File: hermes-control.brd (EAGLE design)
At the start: 106 x 47 mm, 73 parts, among them J1 1981568-1, J3 2201778-1, Q2 BC849SMD, Q3 FDN360P, Q4 FDN360P, Q5 BC849SMD, Q6 MMBT3906SOT23-3, Q7 FDN360P, Q8 MMBT2222A, U1 LSM9DS1TR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

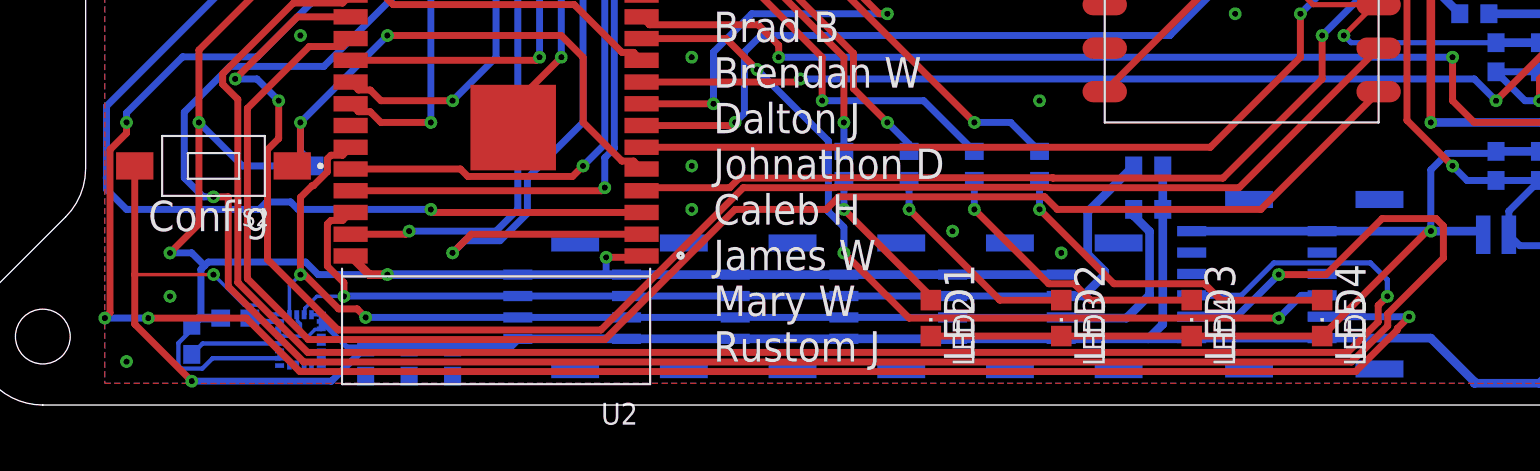
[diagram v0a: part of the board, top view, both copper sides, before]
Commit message: more gnd
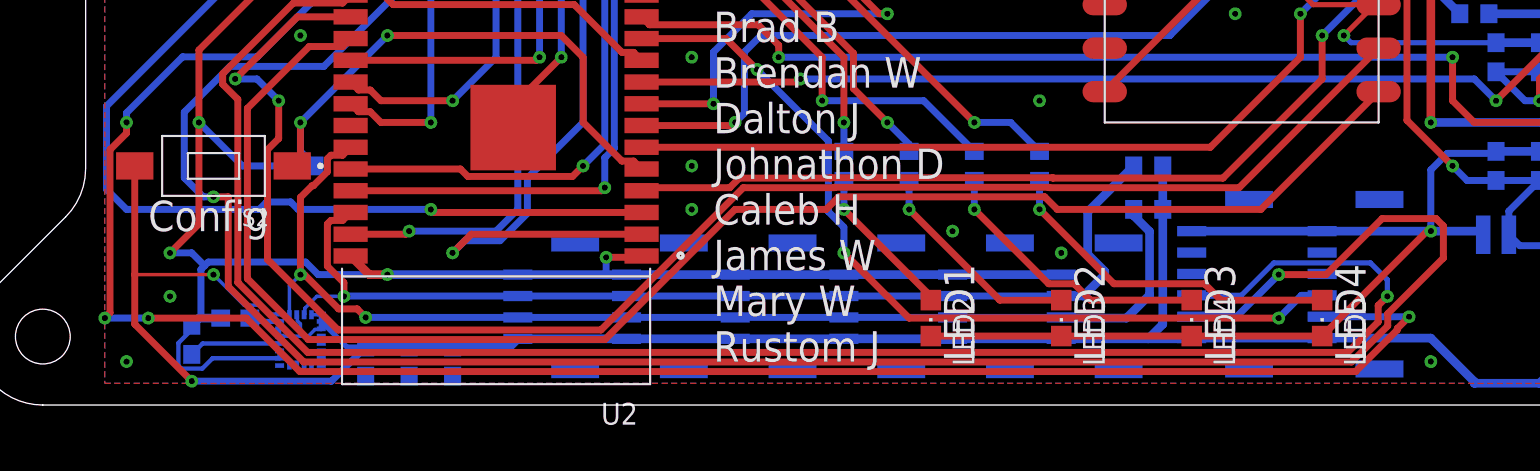
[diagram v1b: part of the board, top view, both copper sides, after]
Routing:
- net GND: vias 46 -> 47
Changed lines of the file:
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@@
 <via x="63.5" y="8.89" extent="1-16" drill="0.35"/>
 <via x="19.05" y="21.59" extent="1-16" drill="0.35"/>
-<wire x1="17.83" y1="2.735" x2="22.86" y2="1.69" width="0" layer="19" extent="16-16"/>
+<via x="85.09" y="2.54" extent="1-16" drill="0.35"/>
 </signal>
 <signal name="3.3V">
@@
 <wire x1="17.08270625" y1="11.8656" x2="16.64710625" y2="11.43" width="0.4064" layer="16"/>
 <wire x1="7.72056875" y1="17.46056875" x2="19.05" y2="28.79" width="0.4064" layer="16"/>
-<wire x1="7.70100625" y1="13.2770875" x2="7.72056875" y2="13.29665" width="0.4064" layer="16"/>
-<wire x1="7.72056875" y1="13.29665" x2="7.72056875" y2="17.46056875" width="0.4064" layer="16"/>
 <wire x1="8.89" y1="11.43" x2="7.72056875" y2="12.59943125" width="0.4064" layer="16"/>
-<wire x1="7.72056875" y1="12.59943125" x2="7.72056875" y2="13.29665" width="0.4064" layer="16"/>
+<wire x1="7.72056875" y1="12.59943125" x2="7.72056875" y2="17.46056875" width="0.4064" layer="16"/>
 </signal>
 <signal name="N$19">

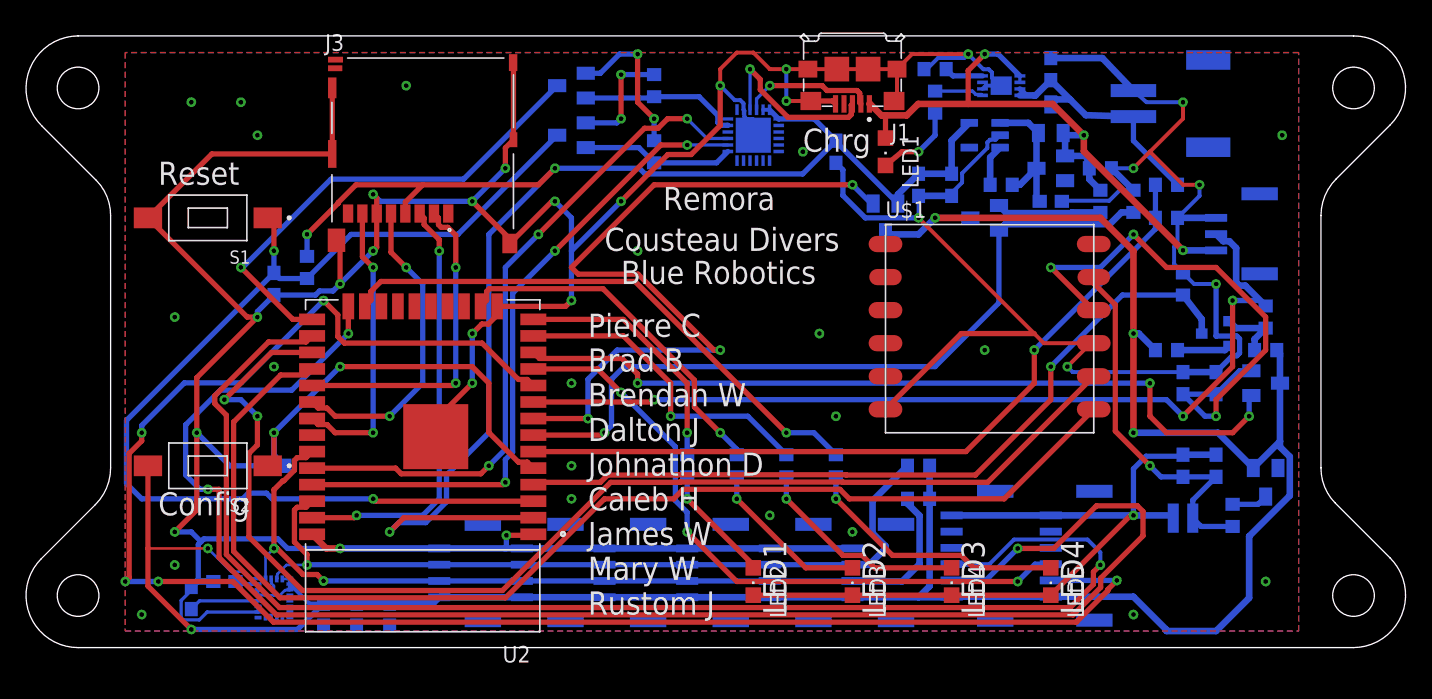
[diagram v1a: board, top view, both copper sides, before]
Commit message: flip sd card and connect vcc to usb uart chip
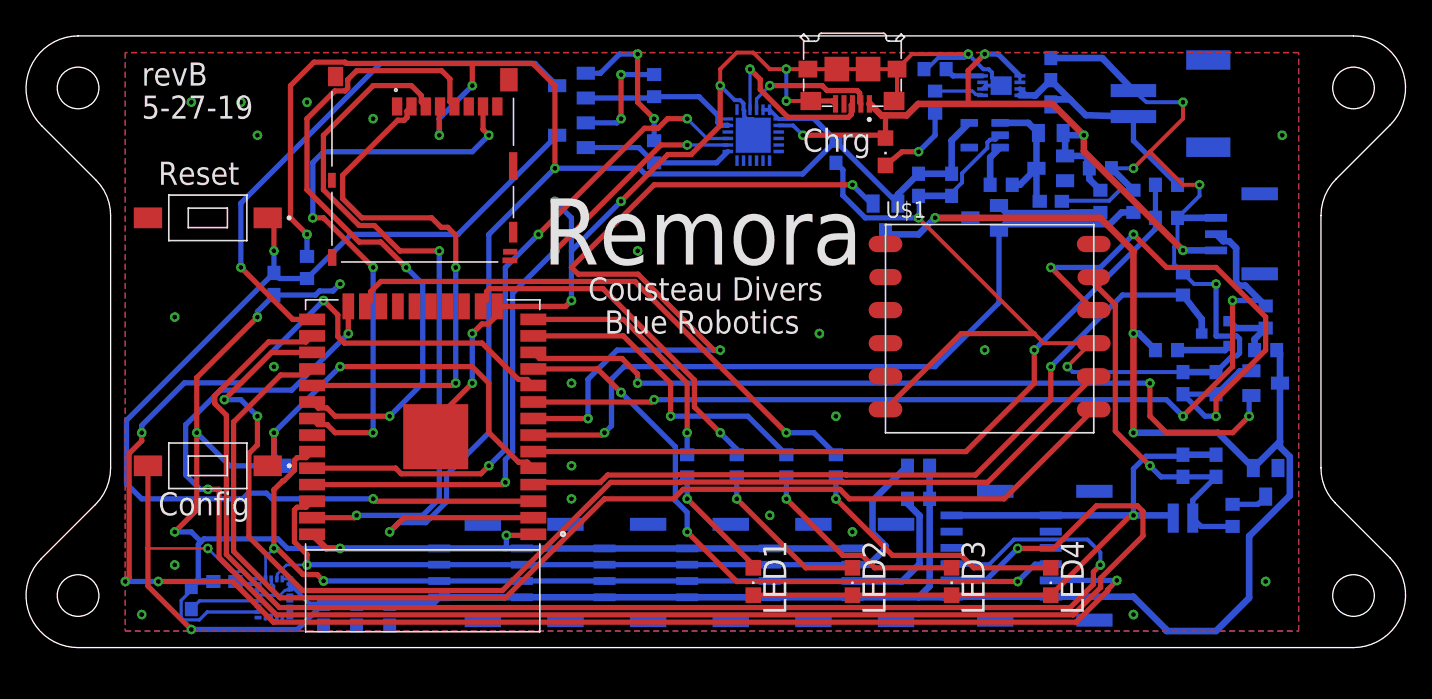
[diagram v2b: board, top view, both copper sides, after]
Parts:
- moved J3 1.27 mm to (30.5, 36.8), turned to 180 degrees
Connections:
- removed net N$11: U3.8
- net VCC: now also U3.8
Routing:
- net GND: track 451.1 -> 377.5 mm, vias 47 -> 43
- net CLK: track 24.0 -> 50.4 mm
- net VCCIO: track 117.7 -> 142.7 mm, vias 3 -> 5
- net MISO: track 22.3 -> 45.1 mm, vias 2 -> 4
- net MOSI: track 32.9 -> 54.9 mm
- net CS: track 25.1 -> 41.9 mm
- net VCC: track 50.9 -> 59.5 mm, vias 3 -> 4
- net PGM: track 37.2 -> 41.5 mm
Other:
- board text added: "5-27-19"
- board text added: "revB"
- board text removed: "Pierre C Brad B Brendan W Dalton J Johnathon D Caleb H James W Mary W Rustom J"

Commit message: new bat connector
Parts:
- LBAT: value S2B-PH-SM4-TB(LF)(SN) -> B2B-PH-SM4-TB(LF)(SN); device hermes:JST_S2B-PH-SM4-TB(LF)(SN) -> B2B-PH-SM4-TB_LF__SN_:JST_B2B-PH-SM4-TB(LF)(SN)
- moved LBAT 7.73 mm to (92.7, 40.5), turned to 0 degrees
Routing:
- net GND: track 377.5 -> 387.6 mm
- net V_BATT: track 19.9 -> 25.7 mm
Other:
- board text added: "5-31-19"
- board text removed: "5-27-19"
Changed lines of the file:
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@@
 <drawing>
 <settings>
-<setting alwaysvectorfont="no"/>
+<setting alwaysvectorfont="yes"/>
 <setting verticaltext="up"/>
 </settings>
-<grid distance="50" unitdist="mil" unit="mil" style="lines" multiple="1" display="yes" altdistance="5" altunitdist="mil" altunit="mil"/>
+<grid distance="50" unitdist="mil" unit="mm" style="lines" multiple="1" display="yes" altdistance="5" altunitdist="mil" altunit="mm"/>
 <layers>
 <layer number="1" name="Top" color="4" fill="1" visible="yes" active="yes"/>
@@
 <text x="81.28" y="2.54" size="1.778" layer="21" rot="R90">LED4</text>
 <text x="8.89" y="43.18" size="1.778" layer="21">revB</text>
-<text x="8.89" y="40.64" size="1.778" layer="21">5-27-19</text>
+<text x="8.89" y="40.64" size="1.778" layer="21">5-31-19</text>
 </plain>
 <attributes>
@@
 <attribute name="VALUE" x="38.10573125" y="47.506" size="1.270959375" layer="27" rot="R180"/>
 </element>
-<element name="LBAT" library="hermes" package="JST_S2B-PH-SM4-TB(LF)(SN)" value="S2B-PH-SM4-TB(LF)(SN)" x="85.09" y="41.8" smashed="yes" rot="MR270">
-<attribute name="MANUFACTURER" value="JST" x="85.09" y="41.8" size="1.778" layer="28" rot="MR270" display="off"/>
-<attribute name="NAME" x="82.542390625" y="45.67423125" size="1.27278125" layer="26" rot="MR270"/>
-<attribute name="STANDARD" value="Manufacturer Recommendation" x="85.09" y="41.8" size="1.778" layer="28" rot="MR270" display="off"/>
-<attribute name="VALUE" x="95.2087" y="45.55341875" size="1.274540625" layer="28" rot="MR270"/>
+<element name="LBAT" library="B2B-PH-SM4-TB_LF__SN_" package="JST_B2B-PH-SM4-TB(LF)(SN)" value="B2B-PH-SM4-TB(LF)(SN)" x="92.71" y="40.53" smashed="yes" rot="MR0">
+<attribute name="AVAILABILITY" value="Unavailable" x="92.71" y="40.53" size="1.778" layer="28" rot="MR0" display="off"/>
+<attribute name="DESCRIPTION" value=" PH Series 2 Position 2 mm Pitch Surface Mount Top Entry Shrouded Header " x="92.71" y="40.53" size="1.778" layer="28" rot="MR0" display="off"/>
+<attribute name="MF" value="JST Sales" x="92.71" y="40.53" size="1.778" layer="28" rot="MR0" display="off"/>
+<attribute name="MP" value="B2B-PH-SM4-TB_LF__SN_" x="92.71" y="40.53" size="1.778" layer="28" rot="MR0" display="off"/>
+<attribute name="NAME" x="96.58423125" y="43.077609375" size="1.27278125" layer="26" rot="MR0"/>
+<attribute name="PACKAGE" value="None" x="92.71" y="40.53" size="1.778" layer="28" rot="MR0" display="off"/>
+<attribute name="PRICE" value="None" x="92.71" y="40.53" size="1.778" layer="28" rot="MR0" display="off"/>
+<attribute name="VALUE" x="96.46341875" y="30.4113" size="1.274540625" layer="28" rot="MR0"/>
 </element>
 <element name="R24" library="rcl" library_urn="urn:adsk.eagle:library:334" package="R0603" package3d_urn="urn:adsk.eagle:package:23555/3" value="1k" x="69.85" y="41.91" smashed="yes" rot="MR90">
@@
 <wire x1="13.12" y1="5.08" x2="14.39" y2="5.08" width="0.508" layer="16"/>
 <wire x1="13.12" y1="5.08" x2="12.7" y2="4.66" width="0.508" layer="16"/>
-<wire x1="85.09" y1="42.8" x2="82.7" y2="45.3" width="0.508" layer="16"/>
-<wire x1="82.7" y1="45.3" x2="78.74" y2="45.3" width="0.508" layer="16"/>
 <wire x1="84.03105" y1="35.14" x2="85.09" y2="35.14" width="0.3048" layer="16"/>
 <wire x1="83.22625" y1="34.3352" x2="84.03105" y2="35.14" width="0.3048" layer="16"/>
@@
 <via x="85.09" y="36.83" extent="1-16" drill="0.35"/>
 <wire x1="85.09" y1="36.83" x2="86.36" y2="38.1" width="0.3048" layer="1"/>
-<wire x1="86.36" y1="38.1" x2="88.9" y2="40.64" width="0.3048" layer="1"/>
-<wire x1="88.9" y1="40.64" x2="88.9" y2="41.91" width="0.3048" layer="1"/>
-<via x="88.9" y="41.91" extent="1-16" drill="0.35"/>
-<wire x1="88.9" y1="41.91" x2="86.09" y2="41.91" width="0.3048" layer="16"/>
-<wire x1="86.09" y1="41.91" x2="85.09" y2="42.8" width="0.3048" layer="16"/>
+<via x="82.55" y="41.91" extent="1-16" drill="0.35"/>
 <wire x1="88.48" y1="33.02" x2="90.17" y2="34.71" width="0.3048" layer="16"/>
 <wire x1="90.17" y1="34.71" x2="90.17" y2="35.56" width="0.3048" layer="16"/>
@@
 <wire x1="90.17" y1="35.56" x2="88.9" y2="35.56" width="0.3048" layer="1"/>
 <wire x1="88.9" y1="35.56" x2="86.36" y2="38.1" width="0.3048" layer="1"/>
+<wire x1="86.36" y1="38.1" x2="82.55" y2="41.91" width="0.3048" layer="1"/>
 <wire x1="71.9248" y1="35.73375" x2="71.9248" y2="36.4498" width="0.3048" layer="16"/>
 <wire x1="71.9248" y1="36.4498" x2="73.8652" y2="38.3902" width="0.3048" layer="16"/>
@@
 <via x="21.59" y="41.91" extent="1-16" drill="0.35"/>
 <via x="95.25" y="5.08" extent="1-16" drill="0.35"/>
-<via x="96.52" y="39.37" extent="1-16" drill="0.35"/>
+<via x="96.52" y="36.83" extent="1-16" drill="0.35"/>
 <via x="60.96" y="24.13" extent="1-16" drill="0.35"/>
 <via x="73.66" y="22.86" extent="1-16" drill="0.35"/>
@@
 <via x="85.09" y="2.54" extent="1-16" drill="0.35"/>
 <via x="26.67" y="40.64" extent="1-16" drill="0.35"/>
+<wire x1="78.74" y1="45.3" x2="82.13" y2="41.91" width="0.508" layer="16"/>
+<wire x1="82.13" y1="41.91" x2="82.55" y2="41.91" width="0.508" layer="16"/>
+<wire x1="82.55" y1="41.91" x2="83.82" y2="41.91" width="0.508" layer="16"/>
+<wire x1="86.5964" y1="44.6864" x2="92.4736" y2="44.6864" width="0.508" layer="16"/>
+<wire x1="92.4736" y1="44.6864" x2="93.98" y2="43.18" width="0.508" layer="16"/>
+<wire x1="93.98" y1="43.18" x2="93.98" y2="40.8" width="0.508" layer="16"/>
+<wire x1="93.98" y1="40.8" x2="93.71" y2="40.53" width="0.508" layer="16"/>
+<wire x1="83.82" y1="41.91" x2="86.5964" y2="44.6864" width="0.508" layer="16"/>
 </signal>
 <signal name="3.3V">
@@
 <contactref element="Q4" pad="3"/>
 <wire x1="78.74" y1="43.6" x2="80.22" y2="42.12" width="0.508" layer="16"/>
-<wire x1="80.22" y1="42.12" x2="81.43" y2="40.91" width="0.508" layer="16"/>
-<wire x1="81.43" y1="40.91" x2="85.09" y2="40.8" width="0.508" layer="16"/>
 <wire x1="78.74" y1="41.74" x2="79.12" y2="42.12" width="0.508" layer="16"/>
 <wire x1="79.12" y1="42.12" x2="80.22" y2="42.12" width="0.508" layer="16"/>
@@
 <wire x1="77.47" y1="42.43" x2="76.865" y2="42.43" width="0.4064" layer="16"/>
 <wire x1="76.865" y1="42.43" x2="76.365" y2="42.93" width="0.4064" layer="16"/>
-<wire x1="88.48" y1="35.56" x2="85.09" y2="38.95" width="0.4064" layer="16"/>
-<wire x1="85.09" y1="38.95" x2="85.09" y2="40.8" width="0.4064" layer="16"/>
+<wire x1="82.81" y1="39.53" x2="85.09" y2="39.53" width="0.508" layer="16"/>
+<wire x1="86.36" y1="39.53" x2="90.71" y2="39.53" width="0.508" layer="16"/>
+<wire x1="85.09" y1="39.53" x2="86.36" y2="39.53" width="0.508" layer="16"/>
+<wire x1="90.71" y1="39.53" x2="91.71" y2="40.53" width="0.508" layer="16"/>
+<wire x1="80.22" y1="42.12" x2="82.81" y2="39.53" width="0.508" layer="16"/>
+<wire x1="88.48" y1="35.56" x2="86.36" y2="37.68" width="0.508" layer="16"/>
+<wire x1="86.36" y1="37.68" x2="86.36" y2="39.53" width="0.508" layer="16"/>
 </signal>
 <signal name="VCC">

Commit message: flipped fet
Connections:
- net 3.3V: now also Q3.2; no longer Q3.3
- net N$6: now also Q3.3; no longer Q3.2
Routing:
- net 3.3V: track 201.0 -> 206.0 mm
- net N$6: track 43.3 -> 45.4 mm
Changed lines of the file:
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@@
 <?xml version="1.0" encoding="utf-8"?>
 <!DOCTYPE eagle SYSTEM "eagle.dtd">
-<eagle version="9.4.0">
+<eagle version="9.4.2">
 <drawing>
 <settings>
-<setting alwaysvectorfont="yes"/>
+<setting alwaysvectorfont="no"/>
 <setting verticaltext="up"/>
 </settings>
@@
 <contactref element="U1" pad="6"/>
 <contactref element="U1" pad="5"/>
-<contactref element="Q3" pad="3"/>
 <contactref element="U1" pad="1"/>
 <contactref element="U1" pad="3"/>
@@
 <wire x1="71.08" y1="3.87" x2="68.58" y2="3.87" width="0.508" layer="16"/>
 <wire x1="68.58" y1="3.87" x2="63.5" y2="3.87" width="0.508" layer="16"/>
-<wire x1="96.35" y1="20.32" x2="96.35" y2="15.85" width="0.508" layer="16"/>
-<wire x1="96.35" y1="15.85" x2="94.3" y2="13.8" width="0.508" layer="16"/>
 <wire x1="72.56" y1="33.02" x2="69.85" y2="33.02" width="0.508" layer="16"/>
 <wire x1="69.85" y1="33.02" x2="68.58" y2="31.75" width="0.508" layer="16"/>
@@
 <wire x1="66.04" y1="31.92" x2="66.2164" y2="31.7436" width="0.508" layer="16"/>
 <wire x1="96.1" y1="22.86" x2="96.35" y2="22.61" width="0.508" layer="16"/>
-<wire x1="96.35" y1="22.61" x2="96.35" y2="20.32" width="0.508" layer="16"/>
 <wire x1="69.43" y1="13.97" x2="69.43" y2="11.43" width="0.508" layer="16"/>
 <wire x1="69.43" y1="11.43" x2="69.43" y2="4.72" width="0.508" layer="16"/>
@@
 <wire x1="18.871" y1="4.91553125" x2="19.05" y2="4.73653125" width="0.2032" layer="16"/>
 <wire x1="97.1064" y1="11.6816625" x2="97.1064" y2="14.6683375" width="0.508" layer="16"/>
-<wire x1="96.35" y1="15.85" x2="96.35" y2="15.4247375" width="0.508" layer="16"/>
-<wire x1="97.1064" y1="14.6683375" x2="96.35" y2="15.4247375" width="0.508" layer="16"/>
 <wire x1="94.3" y1="13.8" x2="91.59" y2="16.51" width="0.508" layer="16"/>
 <wire x1="91.59" y1="16.51" x2="85.09" y2="16.51" width="0.508" layer="16"/>
@@
 <wire x1="93.98" y1="8.5552625" x2="97.1064" y2="11.6816625" width="0.508" layer="16"/>
 <wire x1="93.98" y1="3.8115" x2="93.98" y2="8.5552625" width="0.508" layer="16"/>
+<contactref element="Q3" pad="2"/>
+<wire x1="95.74" y1="22.86" x2="96.1" y2="22.86" width="0.4064" layer="16"/>
+<wire x1="94.15" y1="21.27" x2="94.8344" y2="21.9544" width="0.4064" layer="16"/>
+<wire x1="94.8344" y1="21.9544" x2="95.04729375" y2="21.9544" width="0.4064" layer="16"/>
+<wire x1="95.04729375" y1="21.9544" x2="95.2556" y2="22.16270625" width="0.4064" layer="16"/>
+<wire x1="95.2556" y1="22.16270625" x2="95.2556" y2="22.3756" width="0.4064" layer="16"/>
+<wire x1="95.2556" y1="22.3756" x2="95.74" y2="22.86" width="0.4064" layer="16"/>
+<wire x1="96.35" y1="15.4247375" x2="96.35" y2="19.07" width="0.4064" layer="16"/>
+<wire x1="97.19729375" y1="21.1756" x2="97.4056" y2="20.96729375" width="0.4064" layer="16"/>
+<wire x1="97.4056" y1="20.96729375" x2="97.4056" y2="19.67270625" width="0.4064" layer="16"/>
+<wire x1="97.4056" y1="19.67270625" x2="97.19729375" y2="19.4644" width="0.4064" layer="16"/>
+<wire x1="94.15" y1="21.27" x2="94.2444" y2="21.1756" width="0.4064" layer="16"/>
+<wire x1="97.19729375" y1="19.4644" x2="96.7444" y2="19.4644" width="0.4064" layer="16"/>
+<wire x1="96.7444" y1="19.4644" x2="96.35" y2="19.07" width="0.4064" layer="16"/>
+<wire x1="94.2444" y1="21.1756" x2="97.19729375" y2="21.1756" width="0.4064" layer="16"/>
+<wire x1="94.3" y1="13.8" x2="95.9247375" y2="15.4247375" width="0.508" layer="16"/>
+<wire x1="95.9247375" y1="15.4247375" x2="96.35" y2="15.4247375" width="0.508" layer="16"/>
+<wire x1="97.1064" y1="14.6683375" x2="96.35" y2="15.4247375" width="0.508" layer="16"/>
 </signal>
 <signal name="N$1">
@@
 <contactref element="C14" pad="1"/>
 <contactref element="C7" pad="1"/>
-<contactref element="Q3" pad="2"/>
 <wire x1="88.9" y1="19.47" x2="91.44" y2="19.47" width="0.4064" layer="16"/>
-<wire x1="91.44" y1="19.47" x2="93.24" y2="21.27" width="0.4064" layer="16"/>
-<wire x1="93.24" y1="21.27" x2="94.15" y2="21.27" width="0.4064" layer="16"/>
+<wire x1="91.44" y1="19.47" x2="91.865" y2="19.895" width="0.4064" layer="16"/>
 <wire x1="88.9" y1="19.47" x2="90.59" y2="17.78" width="0.4064" layer="16"/>
 <wire x1="90.59" y1="17.78" x2="91.44" y2="17.78" width="0.4064" layer="16"/>
@@
 <wire x1="85.09" y1="31.75" x2="82.55" y2="29.21" width="0.4064" layer="16"/>
 <wire x1="82.55" y1="29.21" x2="78.74" y2="29.21" width="0.4064" layer="16"/>
+<contactref element="Q3" pad="3"/>
+<wire x1="95.925" y1="19.895" x2="96.35" y2="20.32" width="0.4064" layer="16"/>
+<wire x1="93.30270625" y1="20.2256" x2="94.99729375" y2="20.2256" width="0.4064" layer="16"/>
+<wire x1="91.865" y1="19.895" x2="92.97210625" y2="19.895" width="0.4064" layer="16"/>
+<wire x1="95.32789375" y1="19.895" x2="95.925" y2="19.895" width="0.4064" layer="16"/>
+<wire x1="92.97210625" y1="19.895" x2="93.30270625" y2="20.2256" width="0.4064" layer="16"/>
+<wire x1="94.99729375" y1="20.2256" x2="95.32789375" y2="19.895" width="0.4064" layer="16"/>
 </signal>
 <signal name="IO13">
@@
 <signal name="GPS_EN">
 <contactref element="U2" pad="12"/>
-<contactref element="Q3" pad="1"/>
 <via x="46.99" y="20.32" extent="1-16" drill="0.35"/>
 <wire x1="38.98" y1="22.68" x2="39.4444" y2="22.2156" width="0.4064" layer="1"/>
@@
 <wire x1="92.71" y1="16.51" x2="93.98" y2="17.78" width="0.4064" layer="1"/>
 <via x="93.98" y="17.78" extent="1-16" drill="0.35"/>
-<wire x1="93.98" y1="17.78" x2="93.98" y2="19.2" width="0.4064" layer="16"/>
-<wire x1="93.98" y1="19.2" x2="94.15" y2="19.37" width="0.4064" layer="16"/>
+<contactref element="Q3" pad="1"/>
+<wire x1="93.98" y1="17.78" x2="93.98" y2="19.2" width="0.508" layer="16"/>
+<wire x1="93.98" y1="19.2" x2="94.15" y2="19.37" width="0.508" layer="16"/>
 </signal>
 <signal name="PROBE">
